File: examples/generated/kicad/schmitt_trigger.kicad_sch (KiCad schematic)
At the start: 7 parts

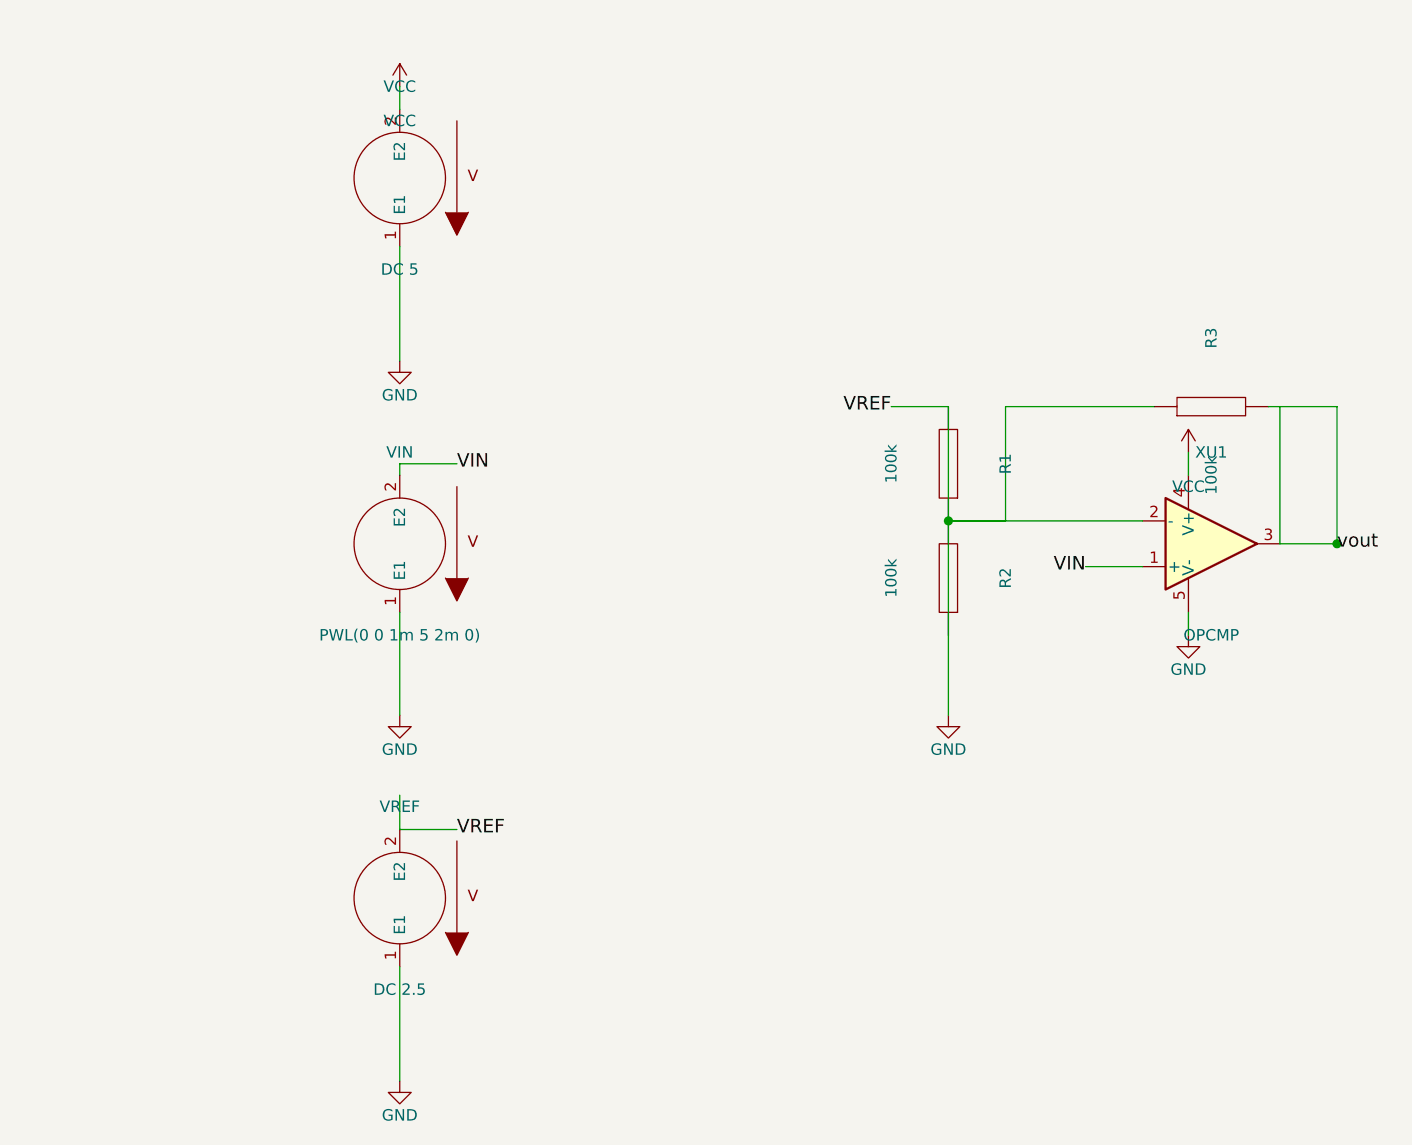
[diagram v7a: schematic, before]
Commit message: Attempt at fixing schmitt trigger wiring.
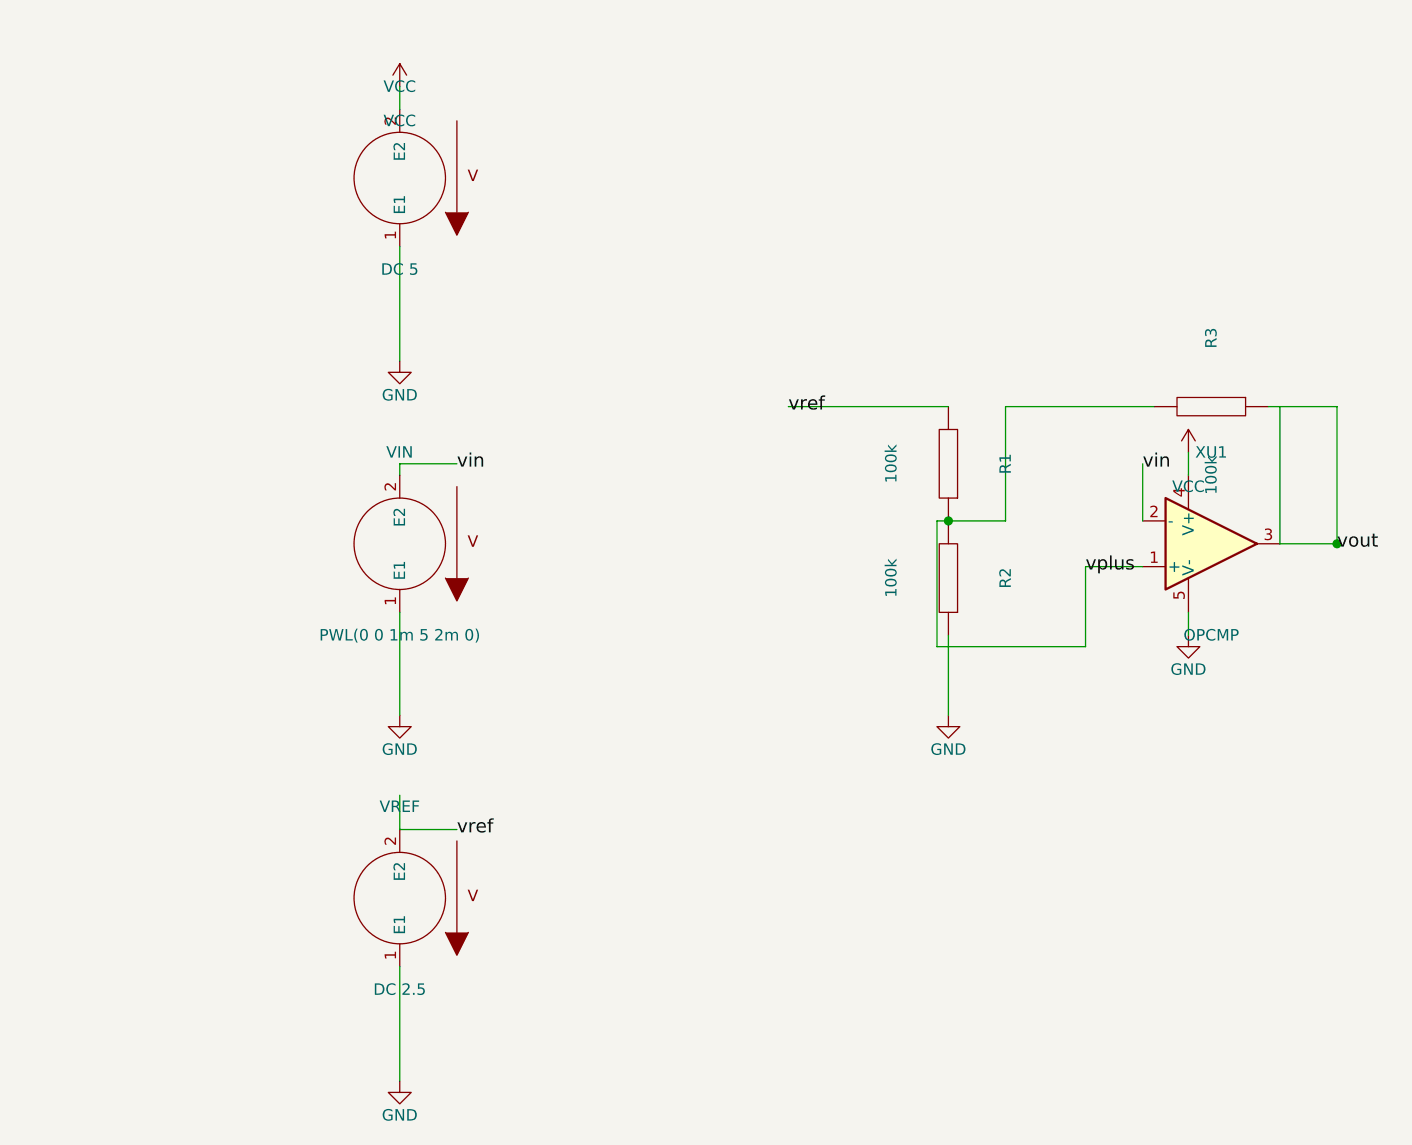
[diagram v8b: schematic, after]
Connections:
- net GND: no longer R1.1, R1.2, R2.2, R3.1, VREF.2 (E2), XU1.2 (-)
- net vout: now also R3.1; no longer R3.2
- net VIN renamed vin
- net vin: now also XU1.2 (-); no longer XU1.1 (+)
- new net vplus: R1.1, R2.2, R3.2, XU1.1 (+)
- new net vref: R1.2, VREF.2 (E2)
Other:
- moved on the sheet: R3
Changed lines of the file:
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@@
     )
   )
-  (symbol (lib_id "R") (at 170.18 85.09 90) (unit 1)
+  (symbol (lib_id "R") (at 170.18 85.09 270) (unit 1)
     (in_bom yes) (on_board yes)
     (property "Reference" "R3" (at 170.18 77.47 0)
@@
     )
   )
-  (label "VIN" (at 86.36 91.44 0)
-    (effects (font (size 1.50 1.50)))
-  )
-  (label "VREF" (at 86.36 132.08 0)
-    (effects (font (size 1.50 1.50)))
-  )
-  (label "VIN" (at 156.21 102.87 180)
-    (effects (font (size 1.50 1.50)))
-  )
-  (label "VREF" (at 134.62 85.09 180)
+  (label "vin" (at 162.56 91.44 0)
+    (effects (font (size 1.50 1.50)))
+  )
+  (label "vin" (at 86.36 91.44 0)
+    (effects (font (size 1.50 1.50)))
+  )
+  (label "vref" (at 123.19 85.09 0)
+    (effects (font (size 1.50 1.50)))
+  )
+  (label "vref" (at 86.36 132.08 0)
+    (effects (font (size 1.50 1.50)))
+  )
+  (label "vplus" (at 156.21 102.87 0)
     (effects (font (size 1.50 1.50)))
   )
@@
     (stroke (width 0) (type solid) (color 0 0 0 0))
   )
+  (wire (pts (xy 162.56 91.44) (xy 162.56 97.79))
+    (stroke (width 0) (type solid) (color 0 0 0 0))
+  )
+  (wire (pts (xy 80.01 132.08) (xy 80.01 128.27))
+    (stroke (width 0) (type solid) (color 0 0 0 0))
+  )
+  (wire (pts (xy 140.97 110.49) (xy 140.97 119.38))
+    (stroke (width 0) (type solid) (color 0 0 0 0))
+  )
+  (wire (pts (xy 123.19 85.09) (xy 140.97 85.09))
+    (stroke (width 0) (type solid) (color 0 0 0 0))
+  )
+  (wire (pts (xy 140.97 97.79) (xy 139.70 97.79))
+    (stroke (width 0) (type solid) (color 0 0 0 0))
+  )
+  (wire (pts (xy 139.70 97.79) (xy 139.70 111.76))
+    (stroke (width 0) (type solid) (color 0 0 0 0))
+  )
+  (wire (pts (xy 139.70 111.76) (xy 156.21 111.76))
+    (stroke (width 0) (type solid) (color 0 0 0 0))
+  )
+  (wire (pts (xy 176.53 85.09) (xy 184.15 85.09))
+    (stroke (width 0) (type solid) (color 0 0 0 0))
+  )
+  (wire (pts (xy 184.15 85.09) (xy 184.15 100.33))
+    (stroke (width 0) (type solid) (color 0 0 0 0))
+  )
+  (wire (pts (xy 163.83 85.09) (xy 147.32 85.09))
+    (stroke (width 0) (type solid) (color 0 0 0 0))
+  )
+  (wire (pts (xy 147.32 85.09) (xy 147.32 97.79))
+    (stroke (width 0) (type solid) (color 0 0 0 0))
+  )
+  (wire (pts (xy 147.32 97.79) (xy 140.97 97.79))
+    (stroke (width 0) (type solid) (color 0 0 0 0))
+  )
+  (wire (pts (xy 80.01 91.44) (xy 86.36 91.44))
+    (stroke (width 0) (type solid) (color 0 0 0 0))
+  )
+  (wire (pts (xy 177.80 100.33) (xy 184.15 100.33))
+    (stroke (width 0) (type solid) (color 0 0 0 0))
+  )
+  (wire (pts (xy 177.80 100.33) (xy 177.80 85.09))
+    (stroke (width 0) (type solid) (color 0 0 0 0))
+  )
+  (wire (pts (xy 156.21 111.76) (xy 156.21 102.87))
+    (stroke (width 0) (type solid) (color 0 0 0 0))
+  )
   (wire (pts (xy 156.21 102.87) (xy 162.56 102.87))
     (stroke (width 0) (type solid) (color 0 0 0 0))
   )
-  (wire (pts (xy 80.01 132.08) (xy 80.01 128.27))
-    (stroke (width 0) (type solid) (color 0 0 0 0))
-  )
-  (wire (pts (xy 140.97 110.49) (xy 140.97 119.38))
-    (stroke (width 0) (type solid) (color 0 0 0 0))
-  )
-  (wire (pts (xy 134.62 85.09) (xy 140.97 85.09))
-    (stroke (width 0) (type solid) (color 0 0 0 0))
-  )
-  (wire (pts (xy 140.97 97.79) (xy 162.56 97.79))
-    (stroke (width 0) (type solid) (color 0 0 0 0))
-  )
-  (wire (pts (xy 140.97 97.79) (xy 140.97 110.49))
-    (stroke (width 0) (type solid) (color 0 0 0 0))
-  )
-  (wire (pts (xy 176.53 85.09) (xy 184.15 85.09))
-    (stroke (width 0) (type solid) (color 0 0 0 0))
-  )
-  (wire (pts (xy 184.15 85.09) (xy 184.15 100.33))
-    (stroke (width 0) (type solid) (color 0 0 0 0))
-  )
-  (wire (pts (xy 163.83 85.09) (xy 147.32 85.09))
-    (stroke (width 0) (type solid) (color 0 0 0 0))
-  )
-  (wire (pts (xy 147.32 85.09) (xy 147.32 97.79))
-    (stroke (width 0) (type solid) (color 0 0 0 0))
-  )
-  (wire (pts (xy 147.32 97.79) (xy 140.97 97.79))
-    (stroke (width 0) (type solid) (color 0 0 0 0))
-  )
-  (wire (pts (xy 80.01 91.44) (xy 86.36 91.44))
-    (stroke (width 0) (type solid) (color 0 0 0 0))
-  )
-  (wire (pts (xy 140.97 85.09) (xy 140.97 97.79))
-    (stroke (width 0) (type solid) (color 0 0 0 0))
-  )
-  (wire (pts (xy 177.80 100.33) (xy 184.15 100.33))
-    (stroke (width 0) (type solid) (color 0 0 0 0))
-  )
-  (wire (pts (xy 177.80 100.33) (xy 177.80 85.09))
-    (stroke (width 0) (type solid) (color 0 0 0 0))
-  )
